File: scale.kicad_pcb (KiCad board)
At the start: 2 copper layers, 80 x 60 mm, 41 parts, among them Q1 S8050, Q2 S8050, U1 HLK-10M12, U2 LM2576HVS-5, U3 AMS1117-3.3, U4 ESP32-WROOM-32U, U5 LMV358, U6 ADS1115IDGS

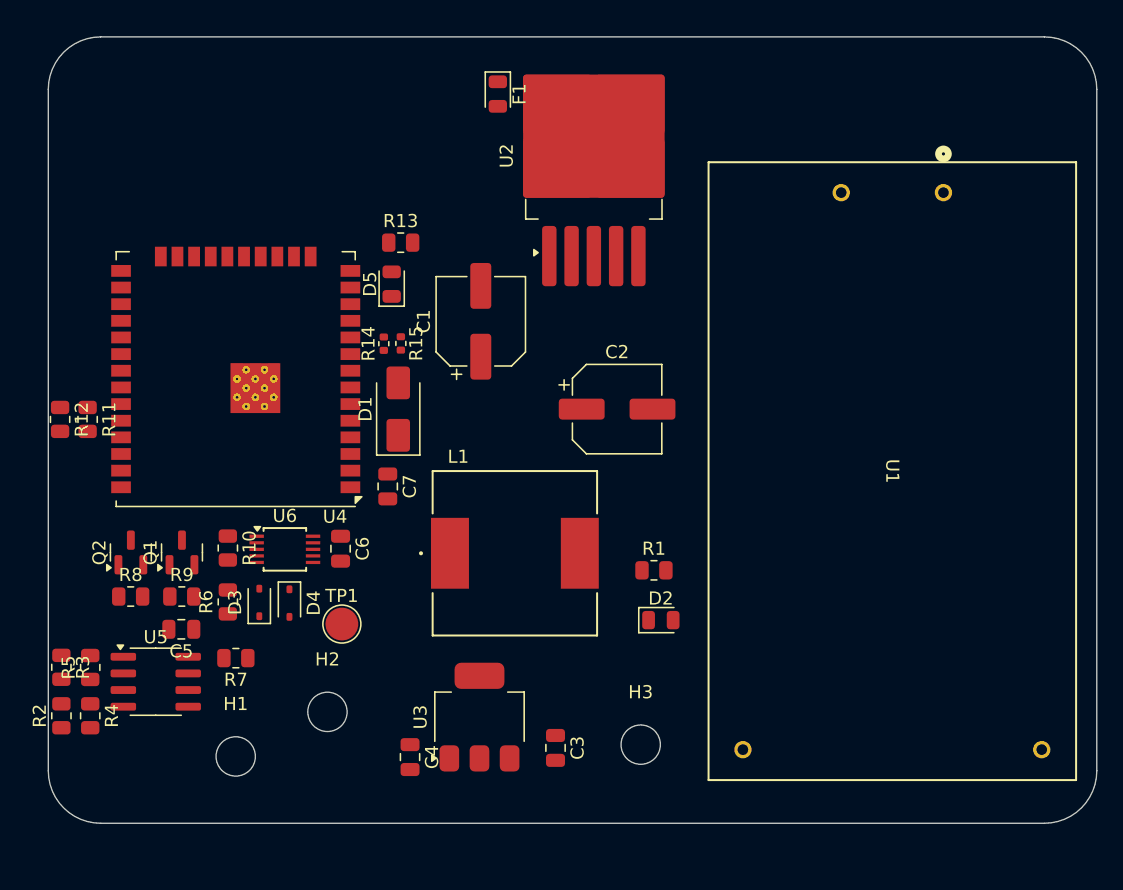
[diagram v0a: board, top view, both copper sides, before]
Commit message: add footprint and step
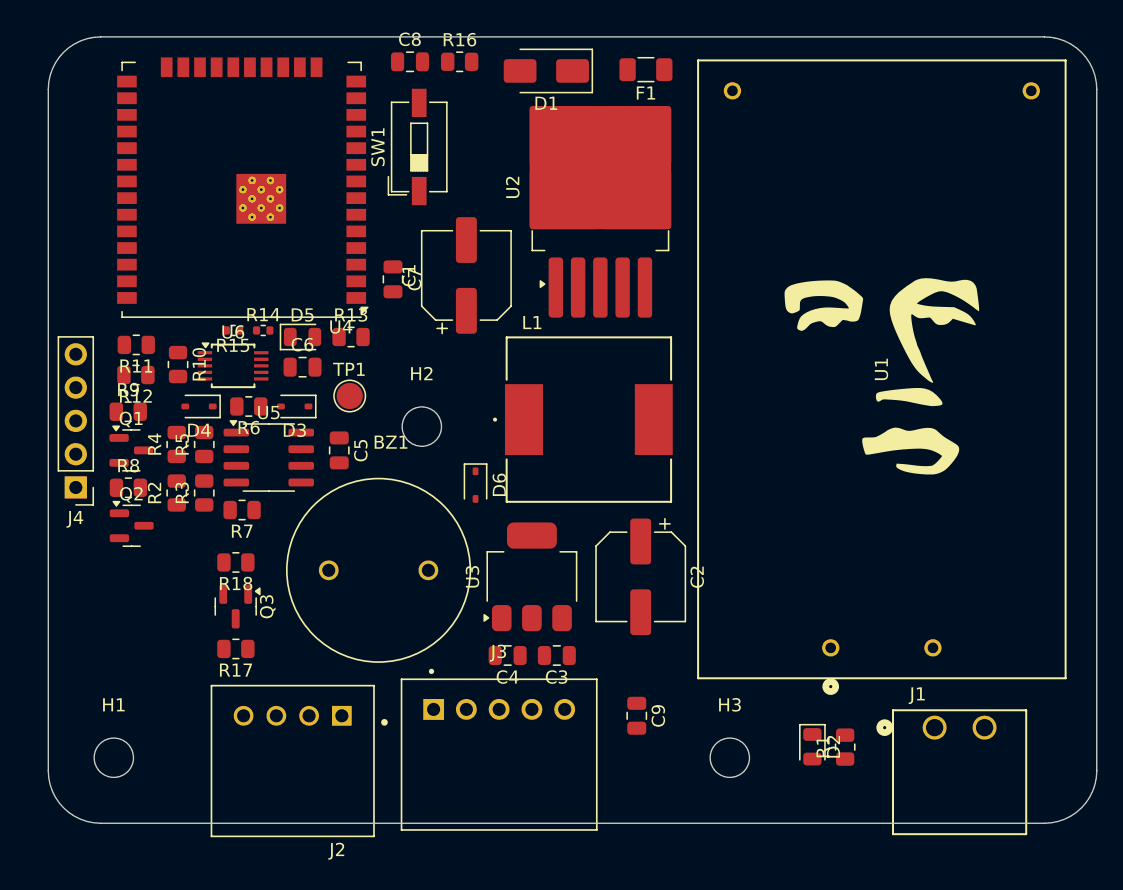
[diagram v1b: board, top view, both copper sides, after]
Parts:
- added BZ1: Buzzer, BBG:buzz_14mm_CUI_CEP-1162, F.Cu at (25.2, 40.7)
- added C8: 100n, Capacitor_SMD:C_0805_2012Metric, F.Cu at (27.6, 1.90)
- added C9: 100n, Capacitor_SMD:C_0805_2012Metric, F.Cu at (44.9, 51.8)
- added D6: BAT60A, Diode_SMD:D_SOD-323, F.Cu at (32.6, 34.2)
- added G***: LOGO, BBG:jkw, F.Cu at (63.7, 26.4)
- added J1: Conn_01x02_Pin, BBG:CONN2_284513-2, F.Cu at (67.6, 52.7)
- added J2: Conn_01x04_Pin, BBG:JST_S4B-XH-A(LF)(SN), F.Cu at (18.6, 51.8)
- added J3: Conn_01x05_Pin, BBG:JST_S5B-XH-A_LF__SN_, F.Cu at (34.4, 51.3)
- added J4: Conn_01x05_Pin, Connector_PinHeader_2.54mm:PinHeader_1x05_P2.54mm_Vertical, F.Cu at (2.10, 34.4)
- added Q3: MMBT3904, Package_TO_SOT_SMD:SOT-23, F.Cu at (14.3, 43.5)
- added R16: 12k, Resistor_SMD:R_0805_2012Metric, F.Cu at (31.4, 1.90)
- added R17: 1k, Resistor_SMD:R_0805_2012Metric, F.Cu at (14.3, 46.7)
- added R18: 1k, Resistor_SMD:R_0805_2012Metric, F.Cu at (14.3, 40.1)
- added SW1: SW_Push, Button_Switch_SMD:SW_DIP_SPSTx01_Slide_6.7x4.1mm_W6.73mm_P2.54mm_LowProfile_JPin, F.Cu at (28.3, 8.40)
- F1: footprint LED_SMD:LED_0805_2012Metric -> Fuse:Fuse_1206_3216Metric
- TP1: footprint TestPoint:TestPoint_Pad_D2.5mm -> TestPoint:TestPoint_Pad_D2.0mm
- moved U1 35.8 mm to (59.7, 46.6), turned to 90 degrees
- moved D1 28.2 mm to (38.0, 2.60), turned to 180 degrees
- moved H2 22.9 mm to (28.5, 29.7)
- moved R4 21.7 mm to (9.80, 31.1), turned to 90 degrees
- moved R1 19.9 mm to (60.8, 54.2), turned to 90 degrees
- moved U5 19.2 mm to (16.8, 32.1)
- moved R2 19.1 mm to (9.80, 34.8)
- moved R5 19.1 mm to (11.9, 31.1)
- moved C5 18.2 mm to (22.2, 31.6), turned to -90 degrees
- moved TP1 17.4 mm to (23.0, 27.4)
- moved R3 17.2 mm to (11.9, 34.8), turned to 90 degrees
- moved D4 16.5 mm to (11.5, 28.2), turned to 180 degrees
- moved C7 15.8 mm to (26.3, 18.5)
- moved D3 15.2 mm to (18.8, 28.2), turned to 180 degrees
- moved D2 15.1 mm to (58.3, 54.2), turned to -90 degrees
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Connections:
- U4 pad 13: unconnected-(U4-IO14-Pad13) -> /display/CLOCK
- U4 pad 14: unconnected-(U4-IO12-Pad14) -> /display/DOT
- U4 pad 16: unconnected-(U4-IO13-Pad16) -> /display/DATA
- U4 pad 29: unconnected-(U4-IO5-Pad29) -> /BUZZ

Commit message: edit board file
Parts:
- moved TP1 3.24 mm to (25.7, 25.6)
- moved C5 0.99 mm to (22.7, 32.4), turned to 0 degrees
- moved R2 0.67 mm to (9.50, 35.4)
- moved R3 0.63 mm to (11.7, 35.4)
- moved R4 0.36 mm to (9.50, 30.9)
- moved R5 0.28 mm to (11.7, 30.9)
- moved J4 0.20 mm to (1.90, 34.4)
- moved D3 0.20 mm to (18.8, 28.0)
- moved D4 0.20 mm to (11.5, 28.0)
- moved R6 0.20 mm to (15.3, 28.0)
- moved J2 0.15 mm to (18.6, 52.0)
- moved SW1 0.10 mm to (28.3, 8.30)
- turned D5 to 180 degrees
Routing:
- net GND: track 0.00 -> 82.2 mm, vias 0 -> 4
- net +5V: track 0.00 -> 53.7 mm, vias 0 -> 1
- net +3V3: track 0.00 -> 49.3 mm, vias 0 -> 2
- net Net-(U2-VIN): track 0.00 -> 43.6 mm, vias 0 -> 2
- net Net-(D1-K): track 0.00 -> 41.3 mm, vias 0 -> 2
- net Net-(U1-+VO): track 0.00 -> 30.5 mm, vias 0 -> 1
- net Net-(BZ1-+): track 0.00 -> 29.3 mm, vias 0 -> 2
- net Net-(BZ1--): track 0.00 -> 26.7 mm, vias 0 -> 2
- net Net-(Q2-B): track 0.00 -> 16.8 mm, vias 0 -> 2
- net GNDA: track 0.00 -> 16.7 mm
- net /power_management/AC_1: track 0.00 -> 13.2 mm
- net /DTR: track 0.00 -> 9.77 mm
- net /power_management/AC_2: track 0.00 -> 9.66 mm
- net /mcu/EN: track 0.00 -> 9.43 mm
- net Net-(D5-A): track 0.00 -> 7.93 mm
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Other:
- copper layers 2 -> 4

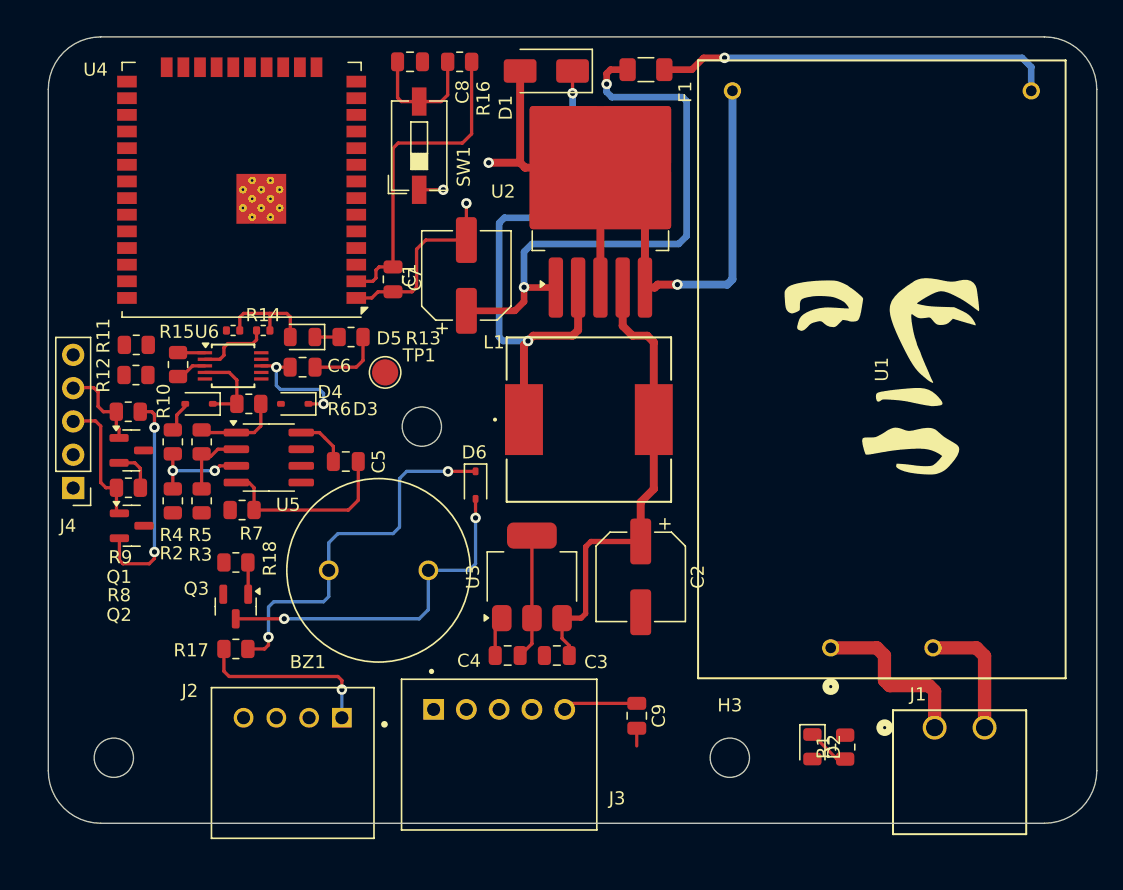
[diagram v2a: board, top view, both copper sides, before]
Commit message: routing some signals: I2C, EN, IO0, BUZZ
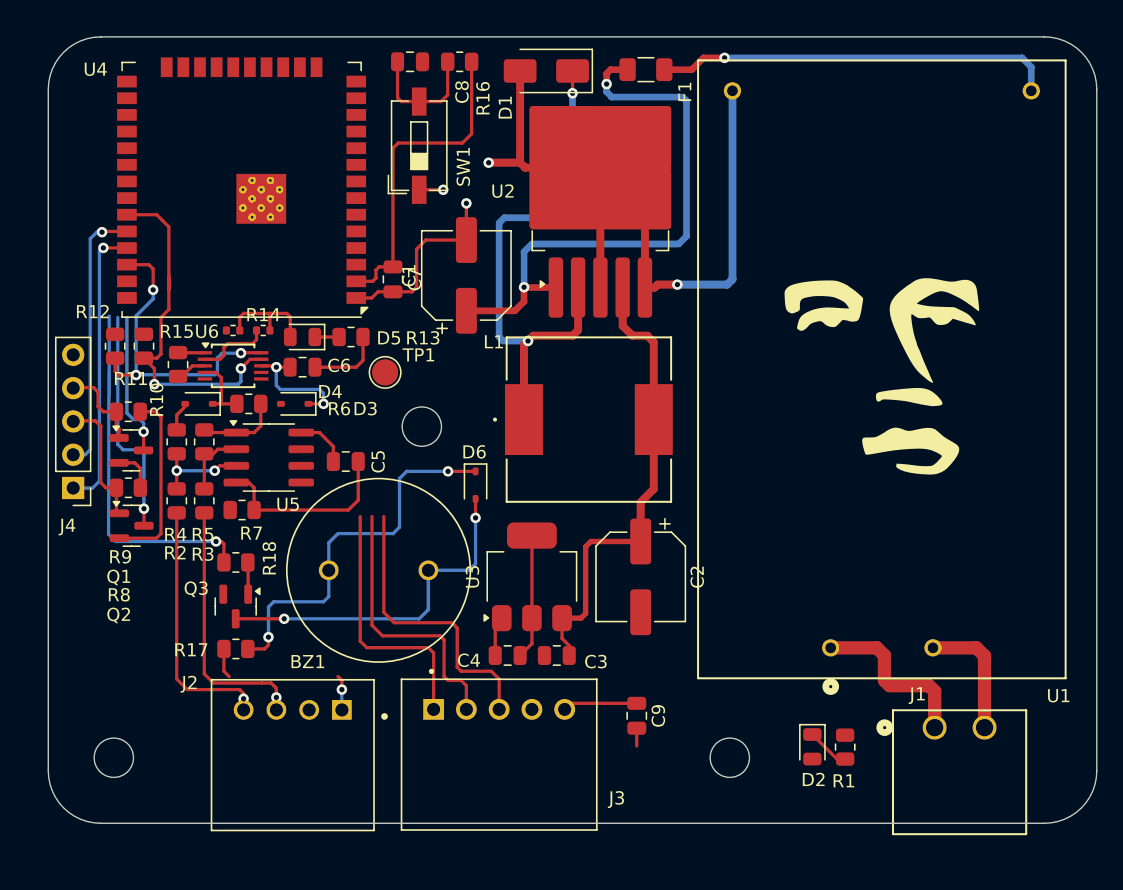
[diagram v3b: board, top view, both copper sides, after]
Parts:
- moved R12 2.71 mm to (5.10, 23.6), turned to 90 degrees
- moved J2 0.60 mm to (18.7, 51.4)
- moved R11 0.60 mm to (7.30, 23.6), turned to 90 degrees
- moved R2 0.30 mm to (9.80, 35.4)
- moved R4 0.30 mm to (9.80, 30.9)
- moved R3 0.20 mm to (11.9, 35.4)
- moved R5 0.20 mm to (11.9, 30.9)
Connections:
- J2 pad 3: /weighing_unit/IN1 -> /weighing_unit/IN2
- J2 pad 4: /weighing_unit/IN2 -> /weighing_unit/IN1
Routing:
- net /mcu/SDA: track 0.00 -> 27.7 mm, vias 0 -> 2
- net /BUZZ: track 0.00 -> 27.2 mm, vias 0 -> 1
- net /mcu/SCL: track 0.00 -> 24.5 mm, vias 0 -> 3
- net /display/CLOCK: track 0.00 -> 22.3 mm
- net /TXD: track 0.00 -> 21.9 mm, vias 0 -> 1
- net /display/DATA: track 0.00 -> 20.9 mm
- net /RXD: track 0.00 -> 20.6 mm, vias 0 -> 1
- net /weighing_unit/IN2: track 0.00 -> 20.5 mm, vias 0 -> 1
- net /weighing_unit/IN1: track 0.00 -> 20.1 mm, vias 0 -> 1
- net /display/DOT: track 0.00 -> 19.8 mm
- net /mcu/IO0: track 0.00 -> 17.5 mm, vias 0 -> 1
- net /mcu/EN: track 9.43 -> 20.4 mm, vias 0 -> 1
- net +5V: track 53.7 -> 45.4 mm
- net Net-(Q2-B): track 16.8 -> 14.0 mm, vias 2 -> 0
- net Net-(D3-A): track 6.33 -> 5.25 mm

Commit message: update some routings
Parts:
- D6: moved to B.Cu
- R16: value 12k -> 10k
- moved TP1 11.8 mm to (28.4, 37.0)
- moved D6 9.81 mm to (25.2, 40.7), turned to 0 degrees
- moved C7 1.35 mm to (26.3, 19.9)
- turned C5 to 180 degrees
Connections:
- U4 pad 12: unconnected-(U4-IO27-Pad12) -> /display/CLOCK
- U4 pad 13: /display/CLOCK -> /display/DATA
- U4 pad 16: /display/DATA -> unconnected-(U4-IO13-Pad16)
- U4 pad 24: /RDY_MCU -> unconnected-(U4-IO2-Pad24)
- U4 pad 31: unconnected-(U4-IO19-Pad31) -> /RDY_MCU
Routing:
- net +3V3: track 49.3 -> 88.7 mm
- net /display/DOT: track 19.8 -> 58.5 mm, vias 0 -> 2
- net /display/DATA: track 20.9 -> 58.3 mm, vias 0 -> 2
- net /mcu/EN: track 20.4 -> 57.4 mm, vias 1 -> 2
- net /display/CLOCK: track 22.3 -> 57.7 mm, vias 0 -> 2
- net +5V: track 45.4 -> 78.4 mm
- net /mcu/IO0: track 17.5 -> 38.3 mm, vias 1 -> 2
- net /RDY_MCU: track 0.00 -> 18.4 mm
- net /BUZZ: track 27.2 -> 42.2 mm, vias 1 -> 2
- net Net-(BZ1-+): track 29.3 -> 14.3 mm, vias 2 -> 1
- net GND: track 82.2 -> 93.4 mm, vias 4 -> 5
- net Net-(BZ1--): track 26.7 -> 20.7 mm, vias 2 -> 1
- net Net-(D3-A): track 5.25 -> 10.8 mm
- net GNDA: track 16.7 -> 13.3 mm, vias 0 -> 4
- added copper zone on In1.Cu, net GNDA
- added copper zone on In2.Cu, net GNDA

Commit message: completing route 1
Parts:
- removed G***: LOGO, BBG:jkw
- removed TP1: TestPoint, TestPoint:TestPoint_Pad_D2.0mm
- moved L1 0.50 mm to (41.2, 29.7)
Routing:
- net GND: track 93.4 -> 158.2 mm, vias 5 -> 10
- net +3V3: track 88.7 -> 150.1 mm, vias 2 -> 6
- net +5V: track 78.4 -> 101.2 mm, vias 1 -> 2
- net /mcu/SDA: track 27.7 -> 32.2 mm
- net GNDA: track 13.3 -> 11.5 mm
- net /display/CLOCK: track 57.7 -> 57.1 mm
- added copper zone on B.Cu, net GND
- added copper zone on F.Cu, net GND
- added copper zone on In1.Cu, net GND
- added copper zone on In2.Cu, net GND
- added copper zone on B.Cu, net GNDA
- added copper zone on F.Cu, net GNDA

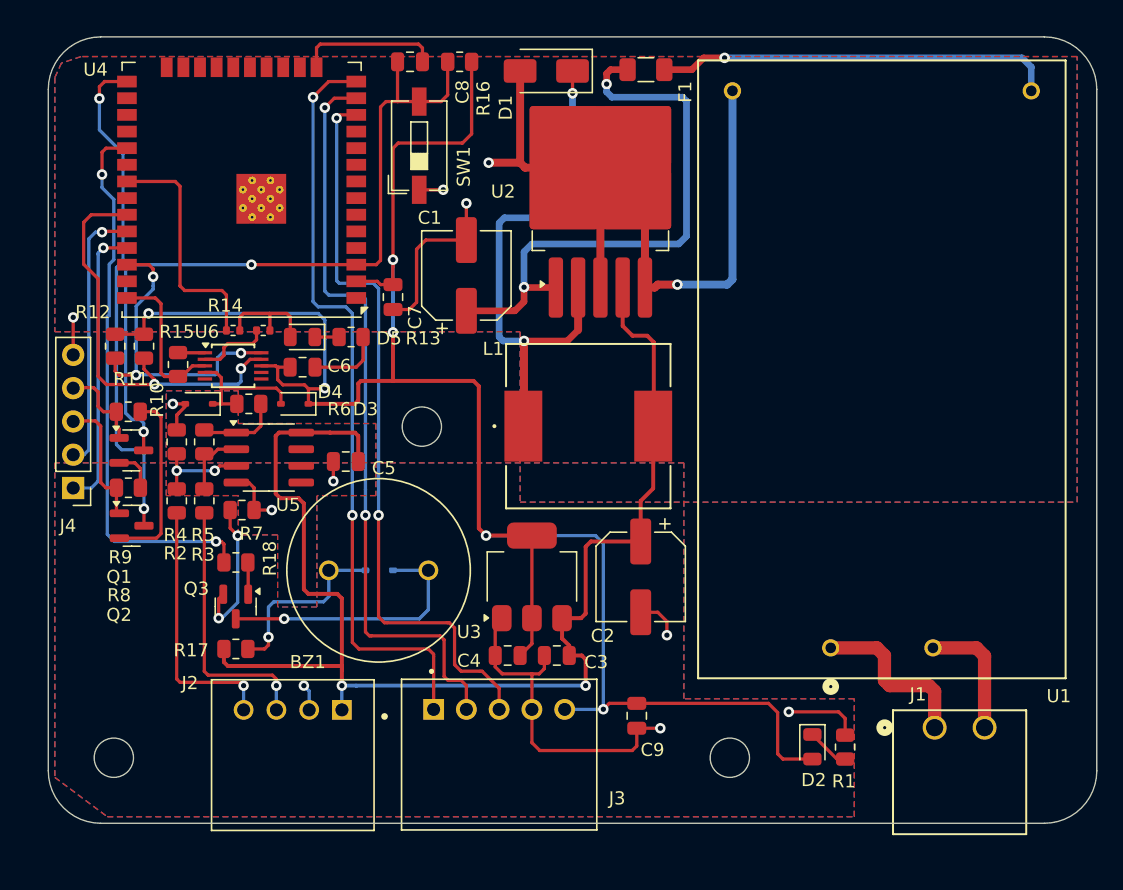
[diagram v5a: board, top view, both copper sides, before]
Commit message: edit copper zone, add pinout address, and reroute EN Signal
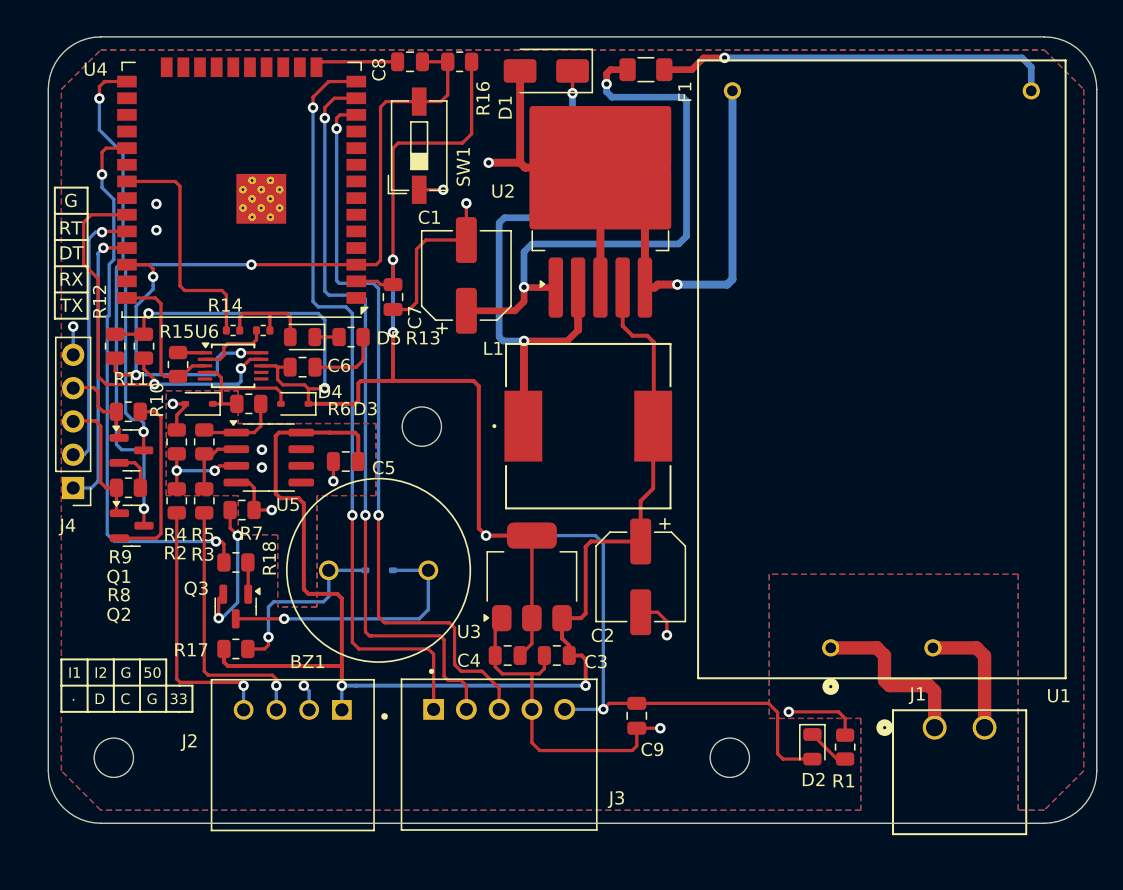
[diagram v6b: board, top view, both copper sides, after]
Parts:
- turned C8 to 180 degrees
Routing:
- net GND: track 158.2 -> 153.0 mm, vias 10 -> 12
- net /mcu/EN: track 57.3 -> 56.2 mm
- net GNDA: vias 4 -> 6
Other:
- board text added: "."
- board text added: "33"
- board text added: "50"
- board text added: "C"
- board text added: "D"
- board text added: "DT"
- board text added: "G"
- board text added: "I1"
- board text added: "I2"
- board text added: "RT"
- board text added: "RX"
- board text added: "TX"
